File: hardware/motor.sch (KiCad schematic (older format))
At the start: 9 parts, among them M1 MOTOR_MOUNTS_AND_ENCODERS, U2 MAX14871, U3 MAX14871

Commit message: updated PCB design
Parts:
- C_MOTOR1, C_MOTOR2: footprint (none) -> Capacitors_SMD:C_0603_HandSoldering
- M1: footprint FUTURA-1.0-MOTOR-MOUNT-TEMPLATE -> footprints_micromouse:FUTURA-1.0-MOTOR-MOUNT-TEMPLATE
- R13, R14: footprint (none) -> Resistors_SMD:R_1206_HandSoldering
- R_MOTOR1, R_MOTOR2: footprint (none) -> Resistors_SMD:R_0603_HandSoldering
- U2, U3: footprint (none) -> Housings_SSOP:TSSOP-16-1EP_4.4x5mm_Pitch0.65mm
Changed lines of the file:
@@
 F 0 "U2" H 3950 3400 60  0000 C CNN
 F 1 "MAX14871" H 3900 2400 60  0000 C CNN
-F 2 "" H 4950 3200 60  0000 C CNN
+F 2 "Housings_SSOP:TSSOP-16-1EP_4.4x5mm_Pitch0.65mm" H 4950 3200 60  0001 C CNN
 F 3 "" H 4950 3200 60  0000 C CNN
 	1    4300 2950
@@
 F 0 "U3" H 3950 5550 60  0000 C CNN
 F 1 "MAX14871" H 3900 4550 60  0000 C CNN
-F 2 "" H 4950 5350 60  0000 C CNN
+F 2 "Housings_SSOP:TSSOP-16-1EP_4.4x5mm_Pitch0.65mm" H 4950 5350 60  0001 C CNN
 F 3 "" H 4950 5350 60  0000 C CNN
 	1    4300 5100
@@
 F 0 "M1" H 6550 4600 45  0001 C CNN
 F 1 "MOTOR_MOUNTS_AND_ENCODERS" H 7400 4350 50  0000 C CNN
-F 2 "FUTURA-1.0-MOTOR-MOUNT-TEMPLATE" H 8100 4600 20  0001 C CNN
+F 2 "footprints_micromouse:FUTURA-1.0-MOTOR-MOUNT-TEMPLATE" H 8100 4600 20  0001 C CNN
 F 3 "" H 7450 3850 60  0000 C CNN
 	1    7450 3900
@@
 Connection ~ 5000 5050
 $Comp
-L GND #PWR13
+L GND #PWR034
 U 1 1 56EB8B5A
 P 6700 4650
-F 0 "#PWR13" H 6700 4400 50  0001 C CNN
+F 0 "#PWR034" H 6700 4400 50  0001 C CNN
 F 1 "GND" H 6700 4500 50  0000 C CNN
 F 2 "" H 6700 4650 50  0000 C CNN
@@
 ~R_FAULT
 $Comp
-L +BATT #PWR6
+L +BATT #PWR035
 U 1 1 56EB8FD2
 P 4250 2000
-F 0 "#PWR6" H 4250 1850 50  0001 C CNN
+F 0 "#PWR035" H 4250 1850 50  0001 C CNN
 F 1 "+BATT" H 4250 2140 50  0000 C CNN
 F 2 "" H 4250 2000 50  0000 C CNN
@@
 $EndComp
 $Comp
-L +5V #PWR12
+L +5V #PWR036
 U 1 1 56EC1082
 P 6600 3200
-F 0 "#PWR12" H 6600 3050 50  0001 C CNN
+F 0 "#PWR036" H 6600 3050 50  0001 C CNN
 F 1 "+5V" H 6600 3340 50  0000 C CNN
 F 2 "" H 6600 3200 50  0000 C CNN
@@
 F 0 "C_MOTOR1" H 4560 2320 50  0000 L CNN
 F 1 "1uF" H 4570 2170 50  0000 L CNN
-F 2 "" H 4550 2250 50  0000 C CNN
+F 2 "Capacitors_SMD:C_0603_HandSoldering" H 4550 2250 50  0001 C CNN
 F 3 "" H 4550 2250 50  0000 C CNN
 	1    4550 2250
@@
 Connection ~ 4350 2250
 $Comp
-L GND #PWR10
+L GND #PWR037
 U 1 1 56ED6D96
 P 4800 2350
-F 0 "#PWR10" H 4800 2100 50  0001 C CNN
+F 0 "#PWR037" H 4800 2100 50  0001 C CNN
 F 1 "GND" H 4800 2200 50  0000 C CNN
 F 2 "" H 4800 2350 50  0000 C CNN
@@
 	4250 2000 4250 2350
 $Comp
-L +BATT #PWR7
+L +BATT #PWR038
 U 1 1 56ED705F
 P 4250 4150
-F 0 "#PWR7" H 4250 4000 50  0001 C CNN
+F 0 "#PWR038" H 4250 4000 50  0001 C CNN
 F 1 "+BATT" H 4250 4290 50  0000 C CNN
 F 2 "" H 4250 4150 50  0000 C CNN
@@
 F 0 "C_MOTOR2" H 4560 4470 50  0000 L CNN
 F 1 "1uF" H 4570 4320 50  0000 L CNN
-F 2 "" H 4550 4400 50  0000 C CNN
+F 2 "Capacitors_SMD:C_0603_HandSoldering" H 4550 4400 50  0001 C CNN
 F 3 "" H 4550 4400 50  0000 C CNN
 	1    4550 4400
@@
 	4250 4150 4250 4500
 $Comp
-L GND #PWR11
+L GND #PWR039
 U 1 1 56ED709E
 P 4800 4500
-F 0 "#PWR11" H 4800 4250 50  0001 C CNN
+F 0 "#PWR039" H 4800 4250 50  0001 C CNN
 F 1 "GND" H 4800 4350 50  0000 C CNN
 F 2 "" H 4800 4500 50  0000 C CNN
@@
 F 0 "R_MOTOR1" V 3490 2360 50  0000 L CNN
 F 1 "10k" V 3610 2360 50  0000 L CNN
-F 2 "" H 3550 2450 50  0000 C CNN
+F 2 "Resistors_SMD:R_0603_HandSoldering" H 3550 2450 50  0001 C CNN
 F 3 "" H 3550 2450 50  0000 C CNN
 	1    3550 2450
@@
 F 0 "R_MOTOR2" V 3540 4510 50  0000 L CNN
 F 1 "10k" V 3660 4510 50  0000 L CNN
-F 2 "" H 3600 4600 50  0000 C CNN
+F 2 "Resistors_SMD:R_0603_HandSoldering" H 3600 4600 50  0001 C CNN
 F 3 "" H 3600 4600 50  0000 C CNN
 	1    3600 4600
@@
 	3600 4700 3600 5000
 $Comp
-L GND #PWR4
+L GND #PWR040
 U 1 1 56ED82CD
 P 3550 3400
-F 0 "#PWR4" H 3550 3150 50  0001 C CNN
+F 0 "#PWR040" H 3550 3150 50  0001 C CNN
 F 1 "GND" H 3550 3250 50  0000 C CNN
 F 2 "" H 3550 3400 50  0000 C CNN
@@
 	3550 2950 3550 3400
 $Comp
-L +3.3V #PWR2
+L +3.3V #PWR041
 U 1 1 56ED83FC
 P 3150 3350
-F 0 "#PWR2" H 3150 3200 50  0001 C CNN
+F 0 "#PWR041" H 3150 3200 50  0001 C CNN
 F 1 "+3.3V" H 3150 3490 50  0000 C CNN
 F 2 "" H 3150 3350 50  0000 C CNN
@@
 F 0 "R13" V 4940 3410 50  0000 L CNN
 F 1 "62.5m" V 5060 3410 50  0000 L CNN
-F 2 "" H 5000 3500 50  0000 C CNN
+F 2 "Resistors_SMD:R_1206_HandSoldering" H 5000 3500 50  0001 C CNN
 F 3 "" H 5000 3500 50  0000 C CNN
 	1    5000 3500
@@
 F 0 "R14" V 4940 5560 50  0000 L CNN
 F 1 "62.5m" V 5060 5560 50  0000 L CNN
-F 2 "" H 5000 5650 50  0000 C CNN
+F 2 "Resistors_SMD:R_1206_HandSoldering" H 5000 5650 50  0001 C CNN
 F 3 "" H 5000 5650 50  0000 C CNN
 	1    5000 5650
@@
 Connection ~ 4300 5850
 $Comp
-L GND #PWR5
+L GND #PWR042
 U 1 1 56ED9574
 P 3550 5550
-F 0 "#PWR5" H 3550 5300 50  0001 C CNN
+F 0 "#PWR042" H 3550 5300 50  0001 C CNN
 F 1 "GND" H 3550 5400 50  0000 C CNN
 F 2 "" H 3550 5550 50  0000 C CNN
@@
 	3550 5100 3550 5550
 $Comp
-L +3.3V #PWR3
+L +3.3V #PWR043
 U 1 1 56ED957C
 P 3150 5500
-F 0 "#PWR3" H 3150 5350 50  0001 C CNN
+F 0 "#PWR043" H 3150 5350 50  0001 C CNN
 F 1 "+3.3V" H 3150 5640 50  0000 C CNN
 F 2 "" H 3150 5500 50  0000 C CNN
@@
 Connection ~ 3550 5450
 $Comp
-L GNDM #PWR?
+L GNDM #PWR044
 U 1 1 56FA27B2
 P 4300 3750
-F 0 "#PWR?" H 4300 3500 50  0001 C CNN
+F 0 "#PWR044" H 4300 3500 50  0001 C CNN
 F 1 "GNDM" H 4300 3600 50  0000 C CNN
 F 2 "" H 4300 3750 50  0000 C CNN
@@
 $EndComp
 $Comp
-L GNDM #PWR?
+L GNDM #PWR045
 U 1 1 56FA283F
 P 4300 5950
-F 0 "#PWR?" H 4300 5700 50  0001 C CNN
+F 0 "#PWR045" H 4300 5700 50  0001 C CNN
 F 1 "GNDM" H 4300 5800 50  0000 C CNN
 F 2 "" H 4300 5950 50  0000 C CNN

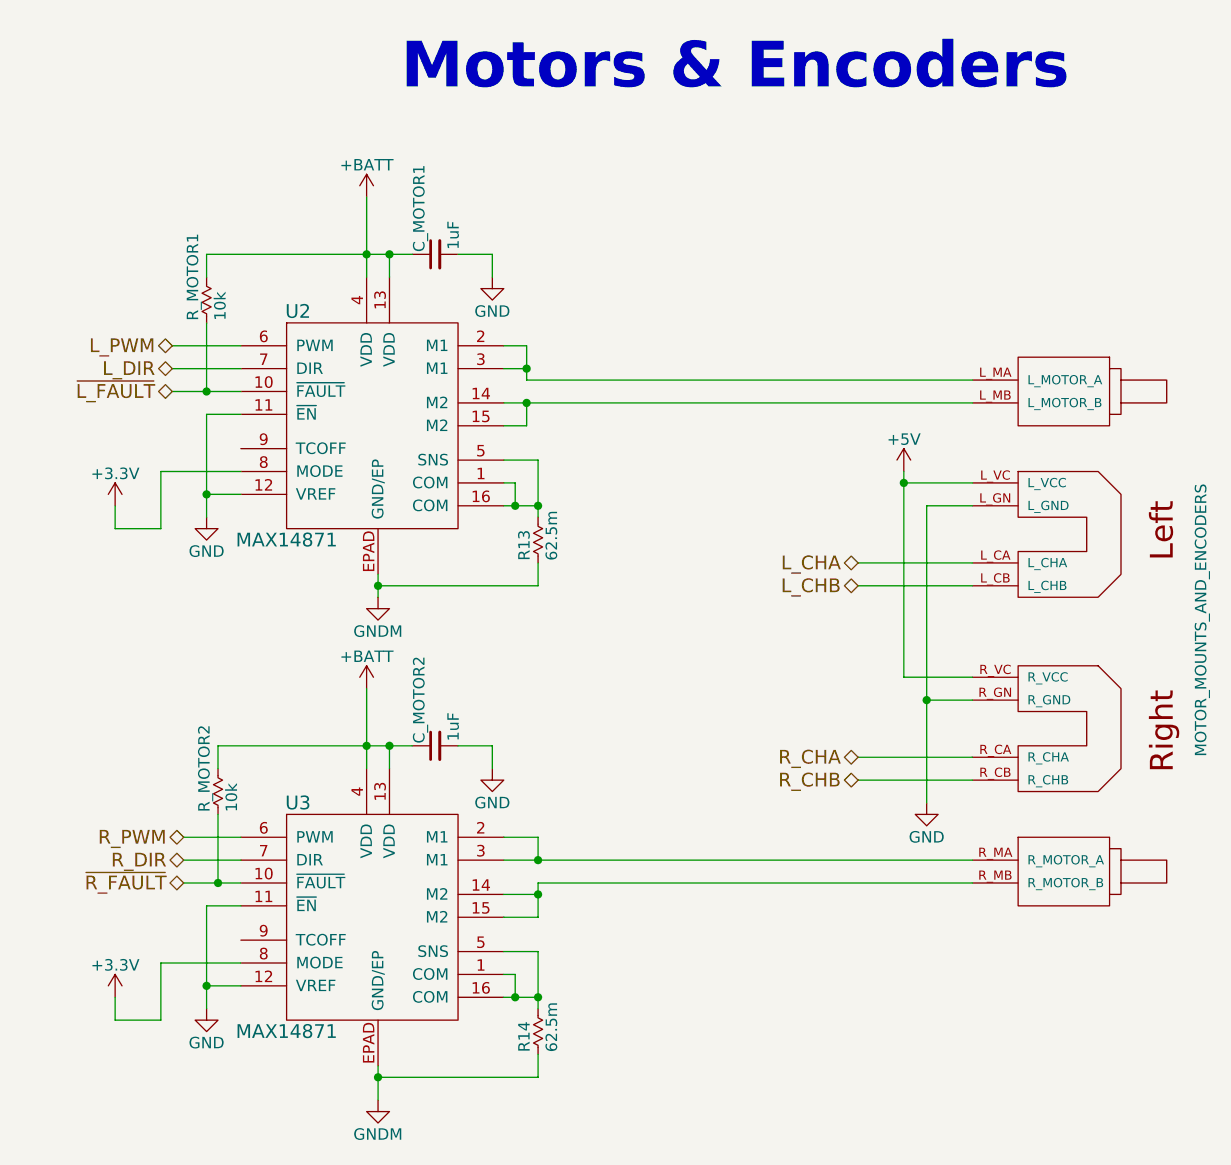
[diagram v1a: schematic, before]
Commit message: PCB board- needs to check the motor driver
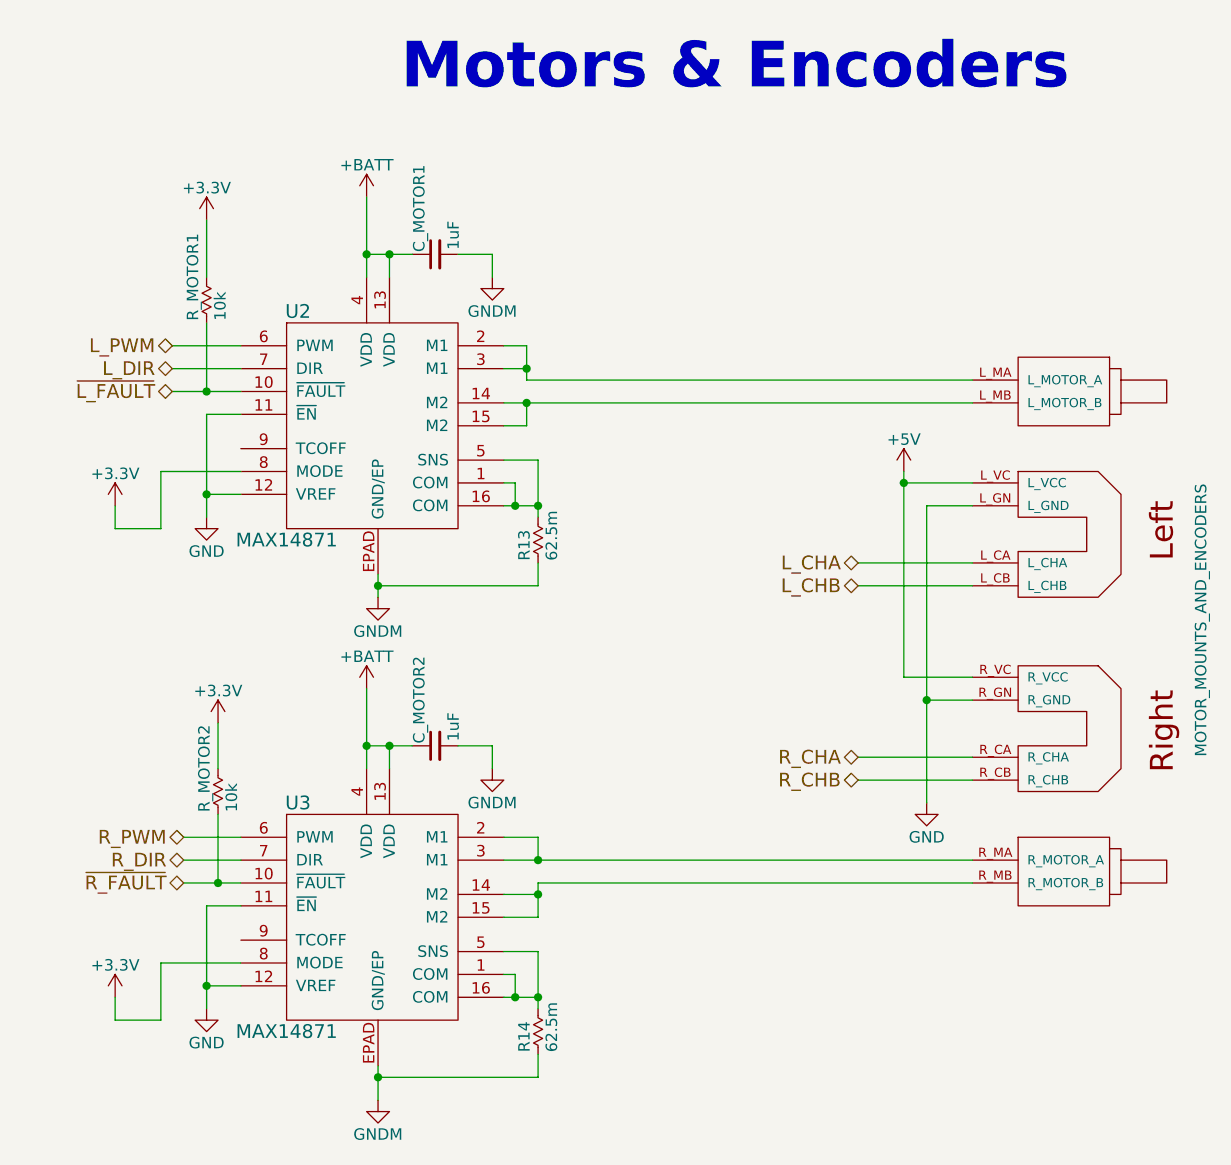
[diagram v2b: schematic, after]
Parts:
- C_MOTOR1, C_MOTOR2: footprint Capacitors_SMD:C_0603_HandSoldering -> Capacitors_SMD:C_0603
- R13, R14: footprint Resistors_SMD:R_1206_HandSoldering -> Resistors_SMD:R_0603
- R_MOTOR1, R_MOTOR2: footprint Resistors_SMD:R_0603_HandSoldering -> Resistors_SMD:R_0603
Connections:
- net +3V3: now also R_MOTOR1.1, R_MOTOR2.1
- net +BATT: no longer R_MOTOR1.1, R_MOTOR2.1
- net GND: no longer C_MOTOR1.2, C_MOTOR2.2
- net GNDM: now also C_MOTOR1.2, C_MOTOR2.2
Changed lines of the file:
@@
 Connection ~ 5000 5050
 $Comp
-L GND #PWR034
+L GND #PWR035
 U 1 1 56EB8B5A
 P 6700 4650
-F 0 "#PWR034" H 6700 4400 50  0001 C CNN
+F 0 "#PWR035" H 6700 4400 50  0001 C CNN
 F 1 "GND" H 6700 4500 50  0000 C CNN
 F 2 "" H 6700 4650 50  0000 C CNN
@@
 ~R_FAULT
 $Comp
-L +BATT #PWR035
+L +BATT #PWR036
 U 1 1 56EB8FD2
 P 4250 2000
-F 0 "#PWR035" H 4250 1850 50  0001 C CNN
+F 0 "#PWR036" H 4250 1850 50  0001 C CNN
 F 1 "+BATT" H 4250 2140 50  0000 C CNN
 F 2 "" H 4250 2000 50  0000 C CNN
@@
 $EndComp
 $Comp
-L +5V #PWR036
+L +5V #PWR037
 U 1 1 56EC1082
 P 6600 3200
-F 0 "#PWR036" H 6600 3050 50  0001 C CNN
+F 0 "#PWR037" H 6600 3050 50  0001 C CNN
 F 1 "+5V" H 6600 3340 50  0000 C CNN
 F 2 "" H 6600 3200 50  0000 C CNN
@@
 F 0 "C_MOTOR1" H 4560 2320 50  0000 L CNN
 F 1 "1uF" H 4570 2170 50  0000 L CNN
-F 2 "Capacitors_SMD:C_0603_HandSoldering" H 4550 2250 50  0001 C CNN
+F 2 "Capacitors_SMD:C_0603" H 4550 2250 50  0001 C CNN
 F 3 "" H 4550 2250 50  0000 C CNN
 	1    4550 2250
 	0    -1   -1   0
 $EndComp
-Wire Wire Line
-	3550 2250 4450 2250
 Connection ~ 4350 2250
-$Comp
-L GND #PWR037
-U 1 1 56ED6D96
-P 4800 2350
-F 0 "#PWR037" H 4800 2100 50  0001 C CNN
-F 1 "GND" H 4800 2200 50  0000 C CNN
-F 2 "" H 4800 2350 50  0000 C CNN
-F 3 "" H 4800 2350 50  0000 C CNN
-	1    4800 2350
-	1    0    0    -1
-$EndComp
 Wire Wire Line
 	4650 2250 4800 2250
@@
 F 0 "C_MOTOR2" H 4560 4470 50  0000 L CNN
 F 1 "1uF" H 4570 4320 50  0000 L CNN
-F 2 "Capacitors_SMD:C_0603_HandSoldering" H 4550 4400 50  0001 C CNN
+F 2 "Capacitors_SMD:C_0603" H 4550 4400 50  0001 C CNN
 F 3 "" H 4550 4400 50  0000 C CNN
 	1    4550 4400
 	0    -1   -1   0
 $EndComp
-Wire Wire Line
-	3600 4400 4450 4400
 Connection ~ 4350 4400
 Wire Wire Line
@@
 Wire Wire Line
 	4250 4150 4250 4500
-$Comp
-L GND #PWR039
-U 1 1 56ED709E
-P 4800 4500
-F 0 "#PWR039" H 4800 4250 50  0001 C CNN
-F 1 "GND" H 4800 4350 50  0000 C CNN
-F 2 "" H 4800 4500 50  0000 C CNN
-F 3 "" H 4800 4500 50  0000 C CNN
-	1    4800 4500
-	1    0    0    -1
-$EndComp
 Connection ~ 4250 2250
 Wire Wire Line
@@
 F 0 "R_MOTOR1" V 3490 2360 50  0000 L CNN
 F 1 "10k" V 3610 2360 50  0000 L CNN
-F 2 "Resistors_SMD:R_0603_HandSoldering" H 3550 2450 50  0001 C CNN
+F 2 "Resistors_SMD:R_0603" H 3550 2450 50  0001 C CNN
 F 3 "" H 3550 2450 50  0000 C CNN
 	1    3550 2450
@@
 $EndComp
 Wire Wire Line
-	3550 2350 3550 2250
+	3550 2100 3550 2350
 Wire Wire Line
 	3550 2550 3550 2850
@@
 F 0 "R_MOTOR2" V 3540 4510 50  0000 L CNN
 F 1 "10k" V 3660 4510 50  0000 L CNN
-F 2 "Resistors_SMD:R_0603_HandSoldering" H 3600 4600 50  0001 C CNN
+F 2 "Resistors_SMD:R_0603" H 3600 4600 50  0001 C CNN
 F 3 "" H 3600 4600 50  0000 C CNN
 	1    3600 4600
@@
 Connection ~ 3600 5000
 Wire Wire Line
-	3600 4400 3600 4500
+	3600 4300 3600 4500
 Wire Wire Line
 	3600 4700 3600 5000
 $Comp
-L GND #PWR040
+L GND #PWR039
 U 1 1 56ED82CD
 P 3550 3400
-F 0 "#PWR040" H 3550 3150 50  0001 C CNN
+F 0 "#PWR039" H 3550 3150 50  0001 C CNN
 F 1 "GND" H 3550 3250 50  0000 C CNN
 F 2 "" H 3550 3400 50  0000 C CNN
@@
 	3550 2950 3550 3400
 $Comp
-L +3.3V #PWR041
+L +3.3V #PWR040
 U 1 1 56ED83FC
 P 3150 3350
-F 0 "#PWR041" H 3150 3200 50  0001 C CNN
+F 0 "#PWR040" H 3150 3200 50  0001 C CNN
 F 1 "+3.3V" H 3150 3490 50  0000 C CNN
 F 2 "" H 3150 3350 50  0000 C CNN
@@
 F 0 "R13" V 4940 3410 50  0000 L CNN
 F 1 "62.5m" V 5060 3410 50  0000 L CNN
-F 2 "Resistors_SMD:R_1206_HandSoldering" H 5000 3500 50  0001 C CNN
+F 2 "Resistors_SMD:R_0603" H 5000 3500 50  0001 C CNN
 F 3 "" H 5000 3500 50  0000 C CNN
 	1    5000 3500
@@
 F 0 "R14" V 4940 5560 50  0000 L CNN
 F 1 "62.5m" V 5060 5560 50  0000 L CNN
-F 2 "Resistors_SMD:R_1206_HandSoldering" H 5000 5650 50  0001 C CNN
+F 2 "Resistors_SMD:R_0603" H 5000 5650 50  0001 C CNN
 F 3 "" H 5000 5650 50  0000 C CNN
 	1    5000 5650
@@
 Connection ~ 4300 5850
 $Comp
-L GND #PWR042
+L GND #PWR041
 U 1 1 56ED9574
 P 3550 5550
-F 0 "#PWR042" H 3550 5300 50  0001 C CNN
+F 0 "#PWR041" H 3550 5300 50  0001 C CNN
 F 1 "GND" H 3550 5400 50  0000 C CNN
 F 2 "" H 3550 5550 50  0000 C CNN
@@
 	3550 5100 3550 5550
 $Comp
-L +3.3V #PWR043
+L +3.3V #PWR042
 U 1 1 56ED957C
 P 3150 5500
-F 0 "#PWR043" H 3150 5350 50  0001 C CNN
+F 0 "#PWR042" H 3150 5350 50  0001 C CNN
 F 1 "+3.3V" H 3150 5640 50  0000 C CNN
 F 2 "" H 3150 5500 50  0000 C CNN
@@
 Connection ~ 3550 5450
 $Comp
-L GNDM #PWR044
+L GNDM #PWR043
 U 1 1 56FA27B2
 P 4300 3750
-F 0 "#PWR044" H 4300 3500 50  0001 C CNN
+F 0 "#PWR043" H 4300 3500 50  0001 C CNN
 F 1 "GNDM" H 4300 3600 50  0000 C CNN
 F 2 "" H 4300 3750 50  0000 C CNN
@@
 $EndComp
 $Comp
-L GNDM #PWR045
+L GNDM #PWR044
 U 1 1 56FA283F
 P 4300 5950
-F 0 "#PWR045" H 4300 5700 50  0001 C CNN
+F 0 "#PWR044" H 4300 5700 50  0001 C CNN
 F 1 "GNDM" H 4300 5800 50  0000 C CNN
 F 2 "" H 4300 5950 50  0000 C CNN
@@
 	1    0    0    -1
 $EndComp
+$Comp
+L GNDM #PWR045
+U 1 1 57019AE9
+P 4800 4500
+F 0 "#PWR045" H 4800 4250 50  0001 C CNN
+F 1 "GNDM" H 4800 4350 50  0000 C CNN
+F 2 "" H 4800 4500 50  0000 C CNN
+F 3 "" H 4800 4500 50  0000 C CNN
+	1    4800 4500
+	1    0    0    -1
+$EndComp
+$Comp
+L GNDM #PWR046
+U 1 1 57019B14
+P 4800 2350
+F 0 "#PWR046" H 4800 2100 50  0001 C CNN
+F 1 "GNDM" H 4800 2200 50  0000 C CNN
+F 2 "" H 4800 2350 50  0000 C CNN
+F 3 "" H 4800 2350 50  0000 C CNN
+	1    4800 2350
+	1    0    0    -1
+$EndComp
+Wire Wire Line
+	4250 4400 4450 4400
+$Comp
+L +3.3V #PWR047
+U 1 1 5702029E
+P 3600 4300
+F 0 "#PWR047" H 3600 4150 50  0001 C CNN
+F 1 "+3.3V" H 3600 4440 50  0000 C CNN
+F 2 "" H 3600 4300 50  0000 C CNN
+F 3 "" H 3600 4300 50  0000 C CNN
+	1    3600 4300
+	1    0    0    -1
+$EndComp
+Wire Wire Line
+	4250 2250 4450 2250
+$Comp
+L +3.3V #PWR048
+U 1 1 57020422
+P 3550 2100
+F 0 "#PWR048" H 3550 1950 50  0001 C CNN
+F 1 "+3.3V" H 3550 2240 50  0000 C CNN
+F 2 "" H 3550 2100 50  0000 C CNN
+F 3 "" H 3550 2100 50  0000 C CNN
+	1    3550 2100
+	1    0    0    -1
+$EndComp

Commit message: PCB Completed
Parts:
- U2, U3: footprint Housings_SSOP:TSSOP-16-1EP_4.4x5mm_Pitch0.65mm -> footprints_micromouse:TSSOP-16_EP
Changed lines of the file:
@@
 F 0 "U2" H 3950 3400 60  0000 C CNN
 F 1 "MAX14871" H 3900 2400 60  0000 C CNN
-F 2 "Housings_SSOP:TSSOP-16-1EP_4.4x5mm_Pitch0.65mm" H 4950 3200 60  0001 C CNN
+F 2 "footprints_micromouse:TSSOP-16_EP" H 4950 3200 60  0001 C CNN
 F 3 "" H 4950 3200 60  0000 C CNN
 	1    4300 2950
@@
 F 0 "U3" H 3950 5550 60  0000 C CNN
 F 1 "MAX14871" H 3900 4550 60  0000 C CNN
-F 2 "Housings_SSOP:TSSOP-16-1EP_4.4x5mm_Pitch0.65mm" H 4950 5350 60  0001 C CNN
+F 2 "footprints_micromouse:TSSOP-16_EP" H 4950 5350 60  0001 C CNN
 F 3 "" H 4950 5350 60  0000 C CNN
 	1    4300 5100
